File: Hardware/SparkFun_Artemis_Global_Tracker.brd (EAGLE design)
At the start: 50.8 x 63.5 mm, 220 parts, among them J1 IRIDIUM_9603N, J2 USB-C, J6 U.FL, J7 ANTENNA-GROUNDEDEDGE_SMA, J8 STANDOFFS_M2X0.4_STEEL_6MM, J9 STANDOFFS_M2X0.4_STEEL_6MM, Q1 5.8A/30V/35mΩ, Q2 20V/4.2A/52mΩ/1.4W, Q3 20V/4.2A/52mΩ/1.4W, Q4 600mA/40V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

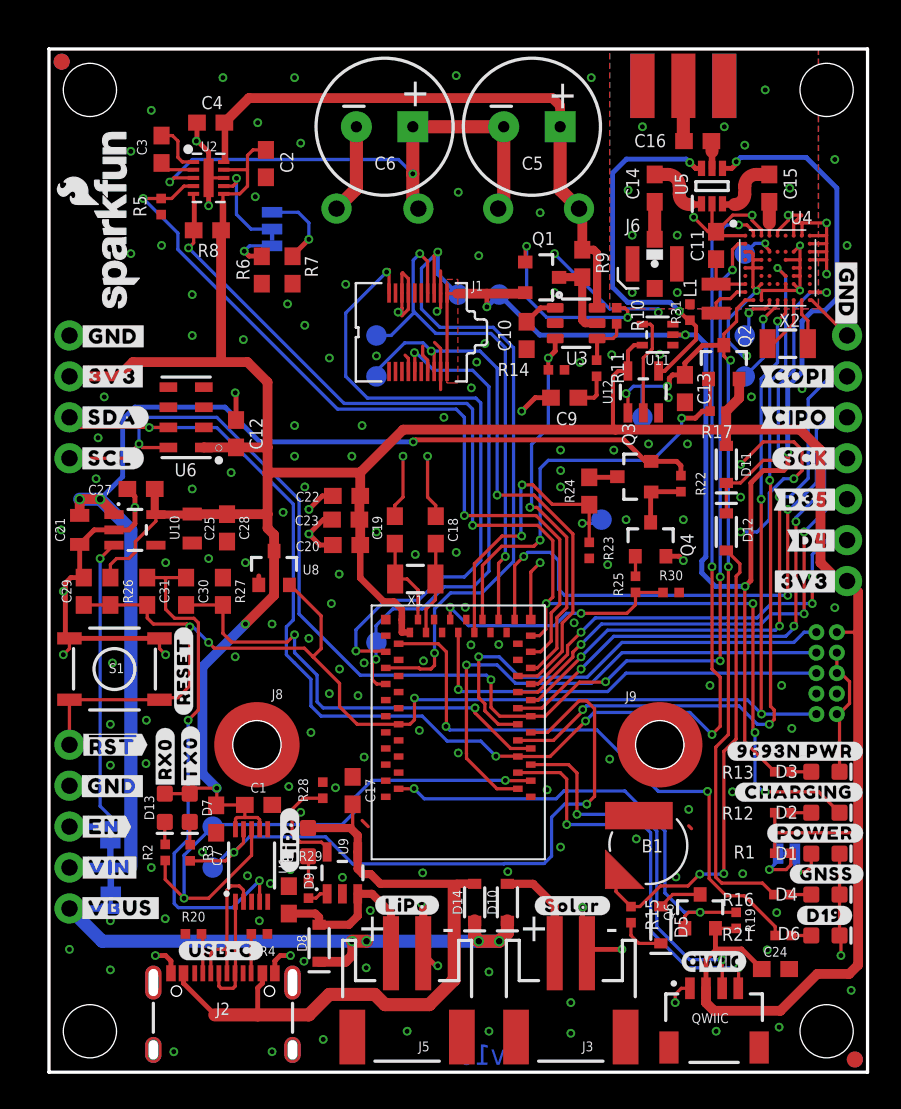
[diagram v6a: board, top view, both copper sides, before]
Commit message: Routed 8 more Artemis GPIOs to PTH headers
-routed AD32, D43, D42, AD31, AD29, AD11, D15 and AD12 to 0.1" PTH headers on upper right edge of board.
-removed full size sparkfun logo, added large flame.
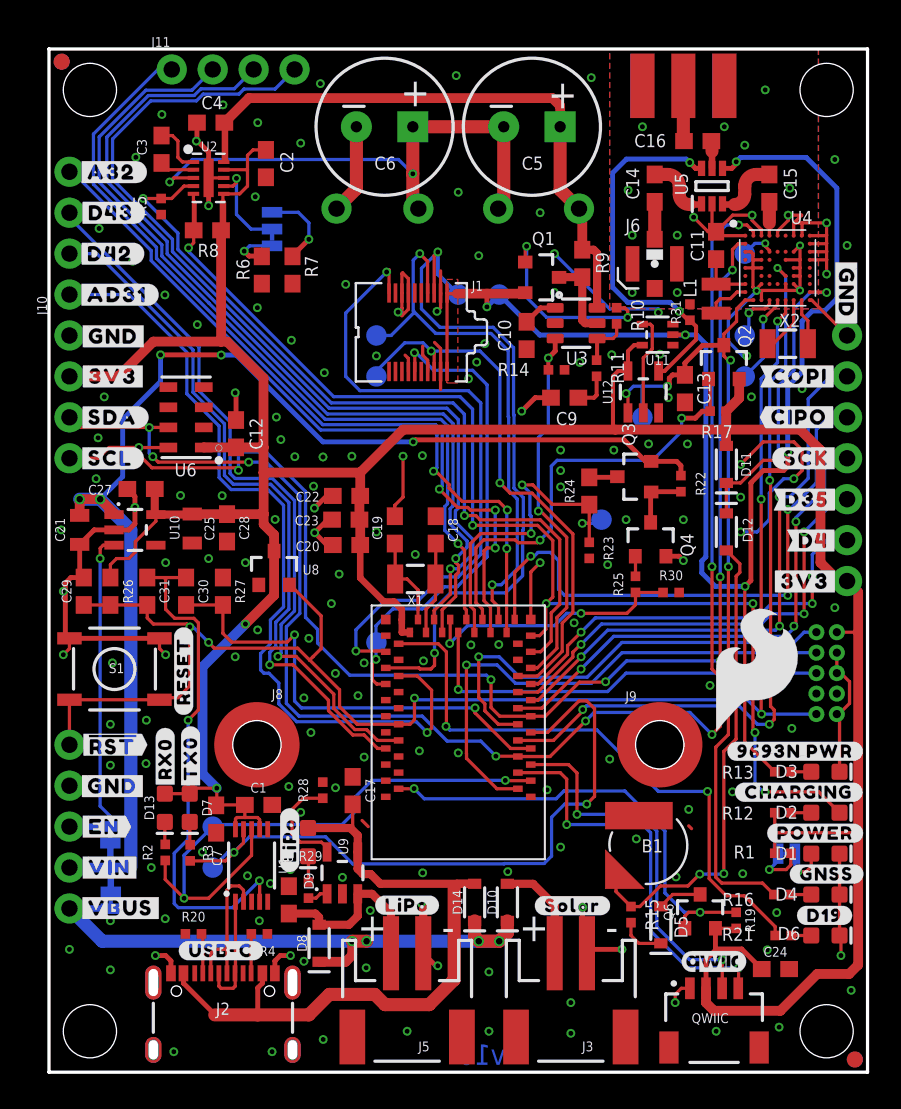
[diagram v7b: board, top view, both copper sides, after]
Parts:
- removed U$72: (no value), output:#150MA#10
- added J10, J11: (no value), SparkFun-Connectors:1X04_NO_SILK
- added U$24: (no value), output:#AD31#7
- added U$71: (no value), output:#D42#32
- added U$73: (no value), output:#D43#43
- added U$79: (no value), output:#A32#44
- added U$80: (no value), output:#MA#45
- added U$81: (no value), output:#60#46
- added U$82: (no value), output:#D43#151
- added U$83: (no value), output:#D42#151
- added U$84: (no value), output:#AD31#151
- added U$85: (no value), output:#AD12#151
- added U$86: (no value), output:#D15#151
- added U$87: (no value), output:#AD11#151
- added U$88: (no value), output:#AD29#151
- added U$89: (no value), output:#CIPO#151
- LOGO2: value SFE_LOGO_NAME_FLAME.1_INCH -> SFE_LOGO_FLAME.3_INCH; device SparkFun-Aesthetics:SFE_LOGO_NAME_FLAME_.1 -> SparkFun-Aesthetics:SFE_LOGO_FLAME_.3
- U$59: device output:#CIPO#9695 -> output:#AD32#152
- U$74: device output:#60MA#151 -> output:#150#61
- moved LOGO2 48.6 mm to (43.9, 24.9), turned to 0 degrees
- moved U$59 44.9 mm to (4.41, 55.9), flipped to the bottom
- moved U$74 7.26 mm to (13.9, 49.2)
- moved U$67 1.25 mm to (9.49, 52.3)
- moved U$31 1.25 mm to (11.0, 52.7)
- moved U$69 1.25 mm to (8.22, 52.2)
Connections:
- new net ARTEMIS_AD11: J11.3, U7.~AD11
- new net ARTEMIS_AD12: J11.1, U7.~AD12
- new net ARTEMIS_AD29: J11.4, U7.~AD29
- new net ARTEMIS_AD31: J10.1, U7.~AD31
- new net ARTEMIS_AD32: J10.4, U7.~AD32
- new net ARTEMIS_D15: J11.2, U7.D15
- new net ARTEMIS_D42: J10.2, U7.~D42
- new net ARTEMIS_D43: J10.3, U7.~D43
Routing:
- net ARTEMIS_AD29: track 0.00 -> 57.9 mm, vias 0 -> 1
- net ARTEMIS_AD11: track 0.00 -> 56.0 mm, vias 0 -> 1
- net ARTEMIS_AD12: track 0.00 -> 54.1 mm, vias 0 -> 3
- net ARTEMIS_D15: track 0.00 -> 52.5 mm, vias 0 -> 1
- net ARTEMIS_AD31: track 0.00 -> 50.7 mm, vias 0 -> 1
- net ARTEMIS_AD32: track 0.00 -> 45.6 mm, vias 0 -> 3
- net ARTEMIS_D43: track 0.00 -> 45.3 mm, vias 0 -> 1
- net ARTEMIS_D42: track 0.00 -> 43.7 mm, vias 0 -> 1
- net GND: track 168.3 -> 162.4 mm, vias 178 -> 175
- net VIN: track 78.0 -> 81.6 mm, vias 3 -> 5
- net ARTEMIS_D9_SDA: track 93.1 -> 95.7 mm, vias 6 -> 8
- net ARTEMIS_D13: track 19.9 -> 21.6 mm
- net ARTEMIS_D17: track 42.5 -> 43.9 mm
- net ARTEMIS_D25: track 33.0 -> 34.3 mm
- net ARTEMIS_D26: track 26.6 -> 27.6 mm
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
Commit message: Broke out D37 to bottom right corner PTH header
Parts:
- added J13: (no value), SparkFun-Connectors:1X01_NO_SILK
- added U$72: (no value), output:#D37#152
- added U$90: (no value), output:#D37#0
- added U$91: (no value), output:#GND#38
- added U$92: (no value), output:##RST##39
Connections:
- new net ARTEMIS_D37: J13.1, U7.~D37
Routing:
- net ARTEMIS_D37: track 0.00 -> 32.5 mm, vias 0 -> 2
- net ARTEMIS_!RTS!: track 32.2 -> 34.7 mm
- net ARTEMIS_RX0: track 36.4 -> 35.4 mm
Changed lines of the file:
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@@
 <element name="U$59" library="output" package="#AD32#152" value="" x="4.41451875" y="55.877459375" smashed="yes" rot="MR0"/>
 <element name="LOGO2" library="SparkFun-Aesthetics" package="SFE_LOGO_FLAME_.3" value="SFE_LOGO_FLAME.3_INCH" x="43.949621875" y="24.9275625" smashed="yes"/>
+<element name="J13" library="SparkFun-Connectors" package="1X01_NO_SILK" value="" x="1.27" y="7.62" smashed="yes">
+<attribute name="NAME" x="0" y="8.763" size="0.6096" layer="25" font="vector" ratio="20"/>
+<attribute name="VALUE" x="0" y="5.842" size="0.6096" layer="27" font="vector" ratio="20"/>
+</element>
+<element name="U$72" library="output" package="#D37#152" value="" x="3.7719" y="7.5692" smashed="yes"/>
+<element name="U$90" library="output" package="#D37#0" value="" x="3.78968125" y="7.56158125" smashed="yes" rot="MR0"/>
+<element name="U$91" library="output" package="#GND#38" value="" x="3.934459375" y="17.7546" smashed="yes" rot="MR0"/>
+<element name="U$92" library="output" package="##RST##39" value="" x="3.94461875" y="20.32508125" smashed="yes" rot="MR0"/>
 </elements>
 <signals>
@@
 <wire x1="19.077940625" y1="58.674" x2="19.077940625" y2="54.828440625" width="0.8128" layer="1"/>
 <wire x1="19.077940625" y1="54.828440625" x2="17.8435" y2="53.594" width="0.8128" layer="1"/>
-<via x="15.621" y="16.129" extent="1-16" drill="0.3"/>
+<via x="15.7861" y="16.273778125" extent="1-16" drill="0.3"/>
 <via x="13.7414" y="11.7094" extent="1-16" drill="0.3"/>
 <via x="14.986" y="7.239" extent="1-16" drill="0.3"/>
@@
 <via x="14.986" y="12.573" extent="1-16" drill="0.3"/>
 <via x="3.81" y="6.35" extent="1-16" drill="0.3"/>
-<via x="1.27" y="7.62" extent="1-16" drill="0.3"/>
-<via x="6.35" y="12.7" extent="1-16" drill="0.3"/>
+<via x="2.659378125" y="6.537959375" extent="1-16" drill="0.3"/>
+<via x="6.0223375" y="12.6619" extent="1-16" drill="0.3"/>
 <via x="3.937" y="25.4" extent="1-16" drill="0.3"/>
 <via x="0.762" y="33.655" extent="1-16" drill="0.3"/>
@@
 <via x="2.921" y="36.83" extent="1-16" drill="0.3"/>
 <via x="3.048" y="39.37" extent="1-16" drill="0.3"/>
-<via x="7.2136" y="9.525" extent="1-16" drill="0.3"/>
+<via x="6.537959375" y="9.0398625" extent="1-16" drill="0.3"/>
 <via x="13.0556" y="9.398" extent="1-16" drill="0.3"/>
 <via x="12.319" y="12.192" extent="1-16" drill="0.3"/>
@@
 <contactref element="RX0" pad="1"/>
 <contactref element="R2" pad="1"/>
-<wire x1="7.2136" y1="13.1398" x2="7.2136" y2="11.9634" width="0.2032" layer="1"/>
-<wire x1="7.2136" y1="11.9634" x2="8.382" y2="10.795" width="0.2032" layer="1"/>
-<via x="8.382" y="10.795" extent="1-16" drill="0.3"/>
-<wire x1="8.382" y1="10.795" x2="8.382" y2="13.462" width="0.2032" layer="16"/>
-<wire x1="8.382" y1="13.462" x2="10.16" y2="15.24" width="0.2032" layer="16"/>
-<wire x1="8.382" y1="10.795" x2="9.906" y2="10.795" width="0.2032" layer="1"/>
-<wire x1="9.906" y1="10.795" x2="12.573" y2="13.462" width="0.2032" layer="1"/>
+<wire x1="7.2136" y1="13.1398" x2="7.2136" y2="12.5603" width="0.2032" layer="1"/>
+<wire x1="7.2136" y1="12.5603" x2="8.689340625" y2="11.084559375" width="0.2032" layer="1"/>
+<via x="8.689340625" y="11.084559375" extent="1-16" drill="0.3"/>
+<wire x1="8.689340625" y1="11.084559375" x2="8.689340625" y2="13.769340625" width="0.2032" layer="16"/>
+<wire x1="8.689340625" y1="13.769340625" x2="10.16" y2="15.24" width="0.2032" layer="16"/>
+<wire x1="8.689340625" y1="11.084559375" x2="10.195559375" y2="11.084559375" width="0.2032" layer="1"/>
+<wire x1="10.195559375" y1="11.084559375" x2="12.573" y2="13.462" width="0.2032" layer="1"/>
 <wire x1="12.573" y1="13.462" x2="12.573" y2="15.077" width="0.2032" layer="1"/>
 <wire x1="18.1864" y1="15.367" x2="10.287" y2="15.367" width="0.2032" layer="16"/>
@@
 <wire x1="13.073" y1="11.8746" x2="13.0604" y2="11.8872" width="0.2032" layer="1"/>
 <via x="13.0604" y="11.8872" extent="1-16" drill="0.3"/>
-<wire x1="13.0604" y1="11.8872" x2="11.384" y2="10.2108" width="0.2032" layer="16"/>
-<wire x1="11.384" y1="10.2108" x2="8.0264" y2="10.2108" width="0.2032" layer="16"/>
-<wire x1="8.0264" y1="10.2108" x2="7.7724" y2="10.4648" width="0.2032" layer="16"/>
-<wire x1="7.7724" y1="13.589" x2="8.636" y2="14.4526" width="0.2032" layer="16"/>
-<wire x1="8.636" y1="14.4526" x2="8.636" y2="21.844" width="0.2032" layer="16"/>
+<wire x1="13.0604" y1="11.8872" x2="10.6093" y2="9.4361" width="0.2032" layer="16"/>
+<wire x1="10.6093" y1="9.4361" x2="7.310115625" y2="9.4361" width="0.2032" layer="16"/>
+<wire x1="7.310115625" y1="9.4361" x2="6.5938375" y2="10.152378125" width="0.2032" layer="16"/>
+<wire x1="6.5938375" y1="16.32965625" x2="8.636" y2="18.37181875" width="0.2032" layer="16"/>
+<wire x1="8.636" y1="18.37181875" x2="8.636" y2="21.844" width="0.2032" layer="16"/>
 <via x="8.636" y="21.844" extent="1-16" drill="0.3"/>
 <wire x1="8.636" y1="21.844" x2="9.271" y2="22.479" width="0.2032" layer="1"/>
-<wire x1="7.7724" y1="10.4648" x2="7.7724" y2="13.589" width="0.2032" layer="16"/>
+<wire x1="6.5938375" y1="10.152378125" x2="6.5938375" y2="16.32965625" width="0.2032" layer="16"/>
 </signal>
 <signal name="ARTEMIS_D8_SCL">
@@
 <wire x1="6.34238125" y1="50.9905" x2="1.45288125" y2="55.88" width="0.2032" layer="16"/>
 </signal>
+<signal name="ARTEMIS_D37">
+<contactref element="U7" pad="~D37"/>
+<via x="23.484840625" y="18.6182" extent="1-16" drill="0.3048"/>
+<wire x1="20.9" y1="18.09" x2="22.42956875" y2="18.09" width="0.2032" layer="1"/>
+<wire x1="22.42956875" y1="18.09" x2="22.44736875" y2="18.1078" width="0.2032" layer="1"/>
+<wire x1="22.974440625" y1="18.1078" x2="23.484840625" y2="18.6182" width="0.2032" layer="1"/>
+<wire x1="22.44736875" y1="18.1078" x2="22.974440625" y2="18.1078" width="0.2032" layer="1"/>
+<wire x1="23.484840625" y1="18.6182" x2="23.307040625" y2="18.4404" width="0.2032" layer="16"/>
+<wire x1="23.307040625" y1="18.4404" x2="19.903825" y2="18.4404" width="0.2032" layer="16"/>
+<wire x1="18.669" y1="17.205575" x2="18.669" y2="16.316959375" width="0.2032" layer="16"/>
+<wire x1="18.669" y1="16.316959375" x2="18.049240625" y2="15.6972" width="0.2032" layer="16"/>
+<wire x1="19.903825" y1="18.4404" x2="18.669" y2="17.205575" width="0.2032" layer="16"/>
+<wire x1="18.049240625" y1="15.6972" x2="10.927078125" y2="15.6972" width="0.2032" layer="16"/>
+<wire x1="10.927078125" y1="15.6972" x2="10.487659375" y2="16.13661875" width="0.2032" layer="16"/>
+<wire x1="10.487659375" y1="16.13661875" x2="9.794240625" y2="16.13661875" width="0.2032" layer="16"/>
+<wire x1="9.0805" y1="14.627475" x2="8.0518" y2="13.598775" width="0.2032" layer="16"/>
+<wire x1="8.0518" y1="13.598775" x2="8.0518" y2="11.249659375" width="0.2032" layer="16"/>
+<wire x1="7.67841875" y1="10.876278125" x2="7.67841875" y2="10.596878125" width="0.2032" layer="16"/>
+<via x="7.67841875" y="10.596878125" extent="1-16" drill="0.3048"/>
+<wire x1="7.67841875" y1="10.596878125" x2="6.73861875" y2="10.596878125" width="0.2032" layer="1"/>
+<wire x1="9.794240625" y1="16.13661875" x2="9.0805" y2="15.422878125" width="0.2032" layer="16"/>
+<wire x1="9.0805" y1="15.422878125" x2="9.0805" y2="14.627475" width="0.2032" layer="16"/>
+<wire x1="8.0518" y1="11.249659375" x2="7.67841875" y2="10.876278125" width="0.2032" layer="16"/>
+<contactref element="J13" pad="1"/>
+<wire x1="3.761740625" y1="7.62" x2="1.27" y2="7.62" width="0.2032" layer="1"/>
+<wire x1="6.73861875" y1="10.596878125" x2="3.761740625" y2="7.62" width="0.2032" layer="1"/>
+</signal>
 </signals>
